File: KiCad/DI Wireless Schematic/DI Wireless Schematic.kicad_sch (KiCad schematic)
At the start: 19 parts

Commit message: Final Schematic
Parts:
- added LS1: Speaker, symbol Device:Speaker
- added Q1: BC327, Package_TO_SOT_THT:TO-92_Inline, symbol Transistor_BJT:BC327
- added Q2: BC337, Package_TO_SOT_THT:TO-92_Inline, symbol Transistor_BJT:BC337
- added Q3: 2N2222, Package_TO_SOT_THT:TO-39-3, symbol Transistor_BJT:2N2219
- added R10, R11: 7.5k, symbol Device:R
- added R2, R3: 1, symbol Device:R
- added R4, R7: 100k, symbol Device:R
- added R5: 22k, symbol Device:R
- added R6, R8: 10k, symbol Device:R
- added R9: 82k, symbol Device:R
- added U1: LM324, symbol Amplifier_Operational:LM324
- added U2: LM358, symbol Amplifier_Operational:LM358
- C1: value C -> 0.22u
- R1: value R -> 130
- V1-LocalOscillator: renamed from V1; value VSIN -> 27 kHz Sine Wave
- V2-LocalOscillator: renamed from V2; value VSIN -> 27 kHz Sine Wave
- V3: value VSIN -> VAUDIO
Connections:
- net GND: now also R11.1, U1.3 (+), U2.3 (+), U2.5 (+)
- net at C1.1, R1.2: now also R6.1
- net at L1.1: now also R2.2; no longer TR2.6
- new net: R6.2, R7.1, U2.2 (-)
- new net: R3.1, R4.2, U1.1
- new net: Q1.2 (B), Q2.2 (B), R3.2
- new net: R8.2, R9.1, U2.6 (-)
- new net: R10.1, R9.2, U2.7
- new net: R7.2, R8.1, U2.1
- new net: R5.2, TR2.6
- new net: Q1.3 (E), Q2.3 (E), R2.1
- new net: R4.1, R5.1, U1.2 (-)
- new net: LS1.1, Q3.1 (E)
- new net: Q3.2 (B), R10.2
- new net: LS1.2, R11.2
- new net VD: Q1.1 (C), Q2.1 (C), Q3.3 (C)
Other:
- note added: "Receiver"
- note removed: "Reciver"
- moved on the sheet: C1, D1, D2, D3, D4, D5, D6, D7, D8, L1, L2, R1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

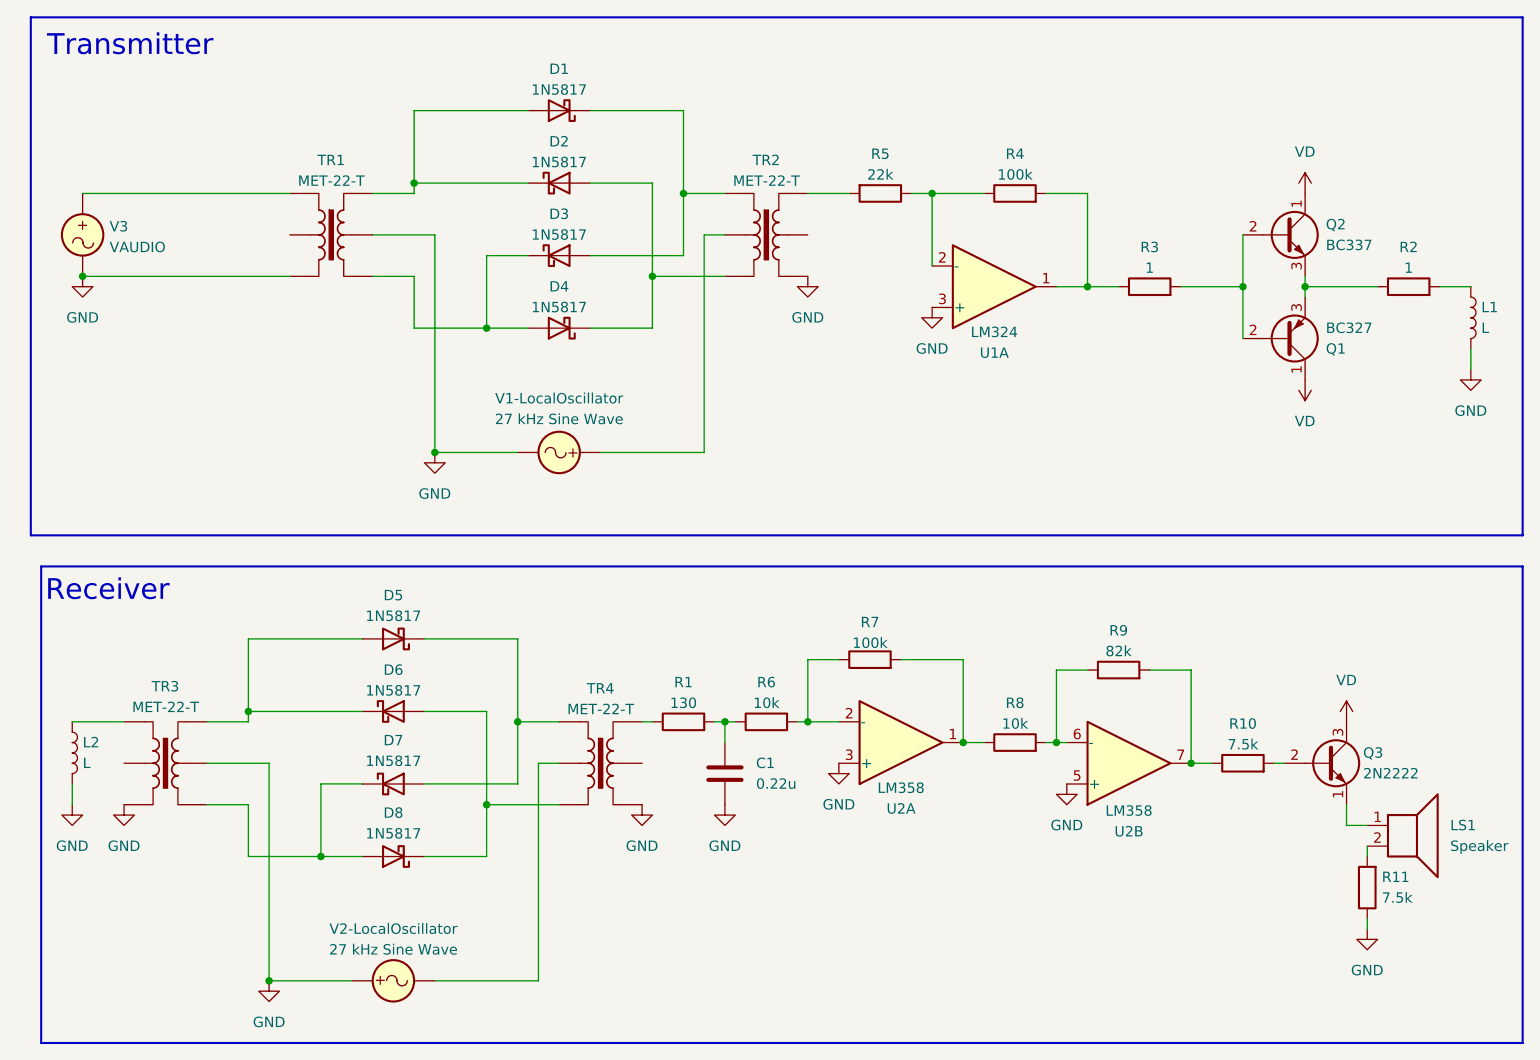
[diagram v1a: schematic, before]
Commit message: fixed voltage rails on schematic
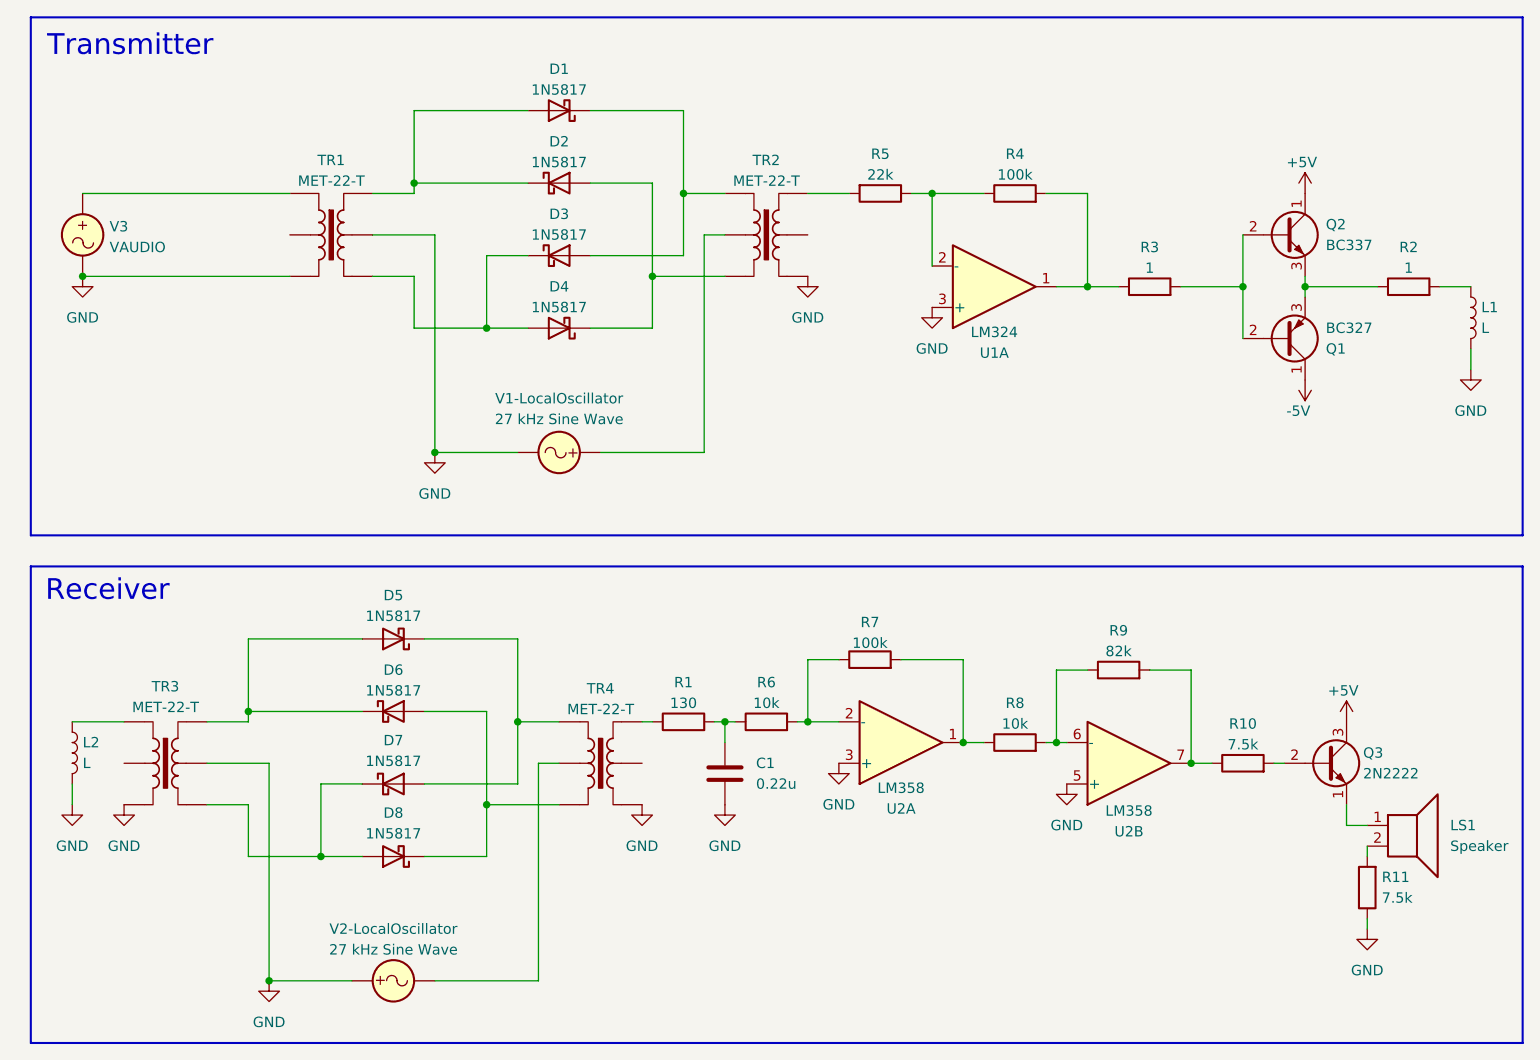
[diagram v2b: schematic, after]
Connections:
- net VD renamed +5V
- net +5V: no longer Q1.1 (C)
- new net -5V: Q1.1 (C)
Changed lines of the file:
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@@
 	)
 	(rectangle
-		(start 19.05 85.09)
+		(start 17.78 85.09)
 		(end 200.66 143.51)
 		(stroke
@@
 		(on_board yes)
 		(dnp no)
-		(fields_autoplaced yes)
 		(property "Reference" "#PWR010"
 			(at 173.99 58.42 0)
@@
 			)
 		)
-		(property "Value" "VD"
-			(at 173.99 67.31 0)
+		(property "Value" "-5V"
+			(at 171.704 66.04 0)
 			(effects
 				(font
 					(size 1.27 1.27)
 				)
+				(justify right)
 			)
 		)
@@
 		(on_board yes)
 		(dnp no)
-		(fields_autoplaced yes)
 		(property "Reference" "#PWR011"
 			(at 173.99 43.18 0)
@@
 			)
 		)
-		(property "Value" "VD"
-			(at 173.99 34.29 0)
+		(property "Value" "+5V"
+			(at 171.704 35.56 0)
 			(effects
 				(font
 					(size 1.27 1.27)
 				)
+				(justify left)
 			)
 		)
@@
 		(on_board yes)
 		(dnp no)
-		(fields_autoplaced yes)
 		(property "Reference" "#PWR015"
 			(at 179.07 107.95 0)
@@
 			)
 		)
-		(property "Value" "VD"
-			(at 179.07 99.06 0)
+		(property "Value" "+5V"
+			(at 176.784 100.33 0)
 			(effects
 				(font
 					(size 1.27 1.27)
 				)
+				(justify left)
 			)
 		)
